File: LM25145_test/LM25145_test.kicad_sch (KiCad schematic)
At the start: 43 parts, among them J1 Conn_01x02_Socket, J2 Conn_01x02_Socket

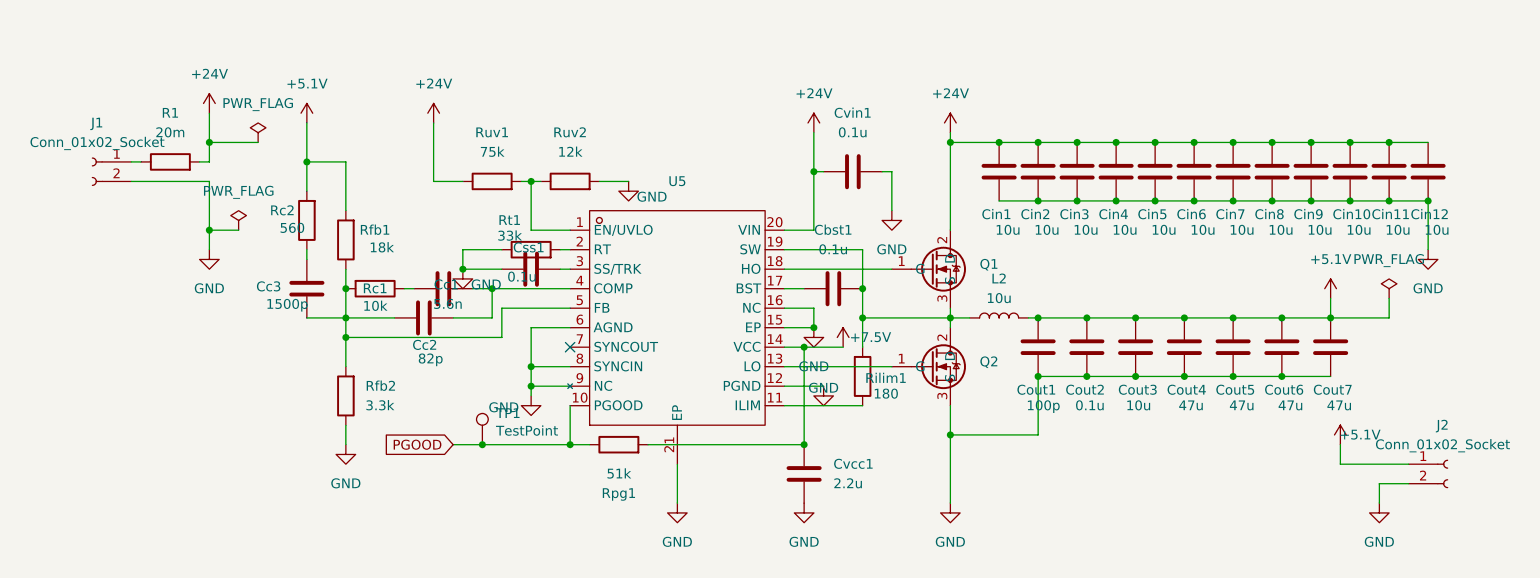
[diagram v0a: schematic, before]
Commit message: LM25145_testの基板サイズを小さくして、発注
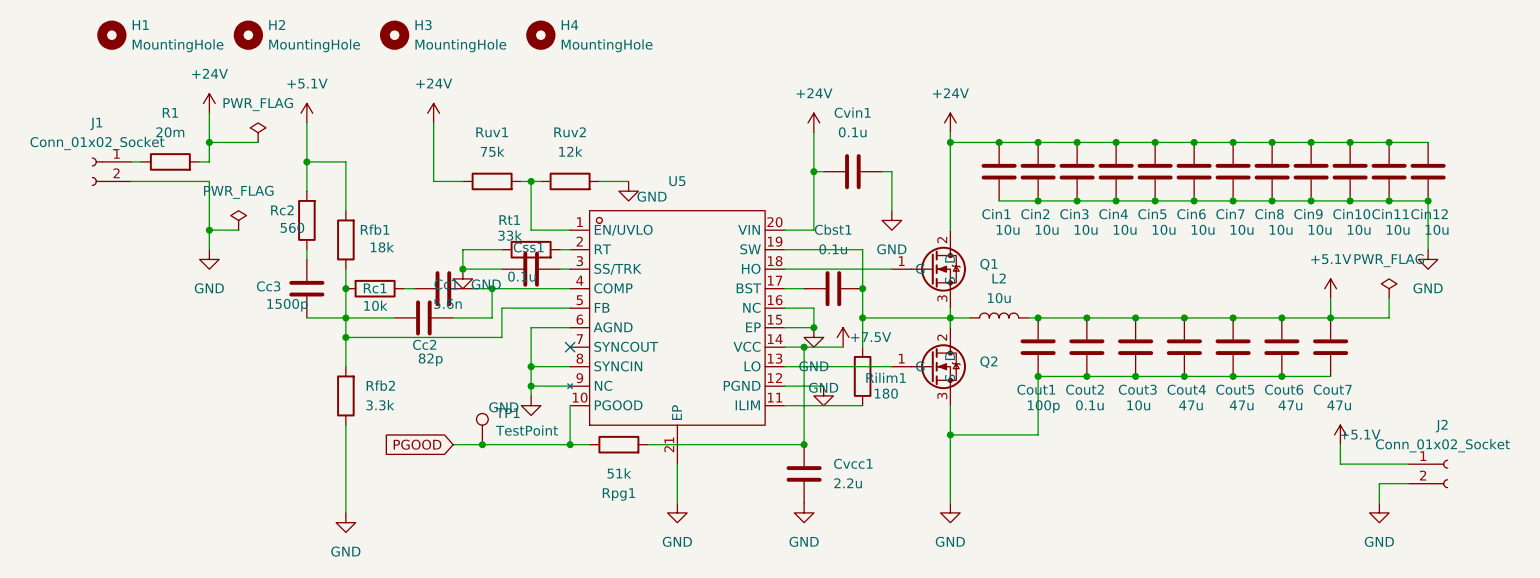
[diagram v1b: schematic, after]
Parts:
- added H1, H2, H3, H4: MountingHole, MountingHole:MountingHole_2.2mm_M2, symbol Mechanical:MountingHole

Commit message: OKL[200~過渡応答を
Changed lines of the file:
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@@
 		)
 		(property "Value" "82p"
-			(at 62.23 70.104 90)
+			(at 61.468 70.612 90)
 			(effects
 				(font

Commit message: 制御基板配線開始
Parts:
- Cout3: value 10u -> 47u
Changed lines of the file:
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@@
 			)
 		)
-		(property "Description" "Unpolarized capacitor"
+		(property "Description" "GRM32ER7YA106KA12"
 			(at 139.7 45.72 0)
 			(effects
@@
 			)
 		)
-		(property "Value" "10u"
+		(property "Value" "47u"
 			(at 151.13 76.2 0)
 			(effects
@@
 			)
 		)
-		(property "Datasheet" "https://akizukidenshi.com/goodsaffix/GRM32ER7YA106KA12.pdf"
+		(property "Datasheet" "https://akizukidenshi.com/goodsaffix/GRM32EC81C476KE15.pdf"
 			(at 152.4 68.58 0)
 			(effects
@@
 			)
 		)
-		(property "Description" "Unpolarized capacitor"
+		(property "Description" "GRM32EC81C476KE15"
 			(at 152.4 68.58 0)
 			(effects
@@
 			)
 		)
-		(property "Description" "Unpolarized capacitor"
+		(property "Description" "GRM32ER7YA106KA12"
 			(at 165.1 45.72 0)
 			(effects
@@
 			)
 		)
-		(property "Description" "Unpolarized capacitor"
+		(property "Description" "GRM32ER7YA106KA12"
 			(at 149.86 45.72 0)
 			(effects
@@
 			)
 		)
-		(property "Description" "Unpolarized capacitor"
+		(property "Description" "GRM32EC81C476KE15"
 			(at 158.75 68.58 0)
 			(effects
@@
 			)
 		)
-		(property "Description" "Unpolarized capacitor"
+		(property "Description" "GRM32ER7YA106KA12"
 			(at 190.5 45.72 0)
 			(effects
@@
 			)
 		)
-		(property "Description" "Unpolarized capacitor"
+		(property "Description" "GRM32ER7YA106KA12"
 			(at 180.34 45.72 0)
 			(effects
@@
 			)
 		)
-		(property "Description" "Unpolarized capacitor"
+		(property "Description" "GRM32ER7YA106KA12"
 			(at 175.26 45.72 0)
 			(effects
@@
 			)
 		)
-		(property "Description" "Unpolarized capacitor"
+		(property "Description" "GRM32ER7YA106KA12"
 			(at 185.42 45.72 0)
 			(effects
@@
 			)
 		)
-		(property "Description" "Unpolarized capacitor"
+		(property "Description" "GRM32ER7YA106KA12"
 			(at 154.94 45.72 0)
 			(effects
@@
 			)
 		)
-		(property "Description" "Unpolarized capacitor"
+		(property "Description" "GRM32ER7YA106KA12"
 			(at 170.18 45.72 0)
 			(effects
@@
 			)
 		)
-		(property "Description" "Inductor"
+		(property "Description" "SMMS1350-100M"
 			(at 134.62 64.77 0)
 			(effects
@@
 			)
 		)
-		(property "Description" "Unpolarized capacitor"
+		(property "Description" "GRM32ER7YA106KA12"
 			(at 144.78 45.72 0)
 			(effects
@@
 			)
 		)
-		(property "Description" "Unpolarized capacitor"
+		(property "Description" "GRM32ER7YA106KA12"
 			(at 160.02 45.72 0)
 			(effects
@@
 			)
 		)
-		(property "Description" "Unpolarized capacitor"
+		(property "Description" "GRM32ER7YA106KA12"
 			(at 134.62 45.72 0)
 			(effects

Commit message: 基板防水REV00発注完了
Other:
- title: (none) -> LM25145_test
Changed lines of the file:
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@@
 	(generator_version "9.0")
 	(paper "A5")
+	(title_block
+		(title "LM25145_test")
+		(rev "00")
+	)
 	(junction
 		(at 78.74 81.28)
